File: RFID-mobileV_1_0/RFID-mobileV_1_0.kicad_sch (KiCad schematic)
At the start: 54 parts, among them J1 USB_C_Receptacle_USB2.0, J2 Conn_01x05_Male, J4 Conn_01x05_Male, Q1 MMBT3904, SW1 SW_Push, U1 XC6206P332MR, U2 E22-400T22S, U3 STM32G030FxP, U4 LM321, U5 DW02, U6 TP4054

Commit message: update
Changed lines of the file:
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@@
+    (stroke (width 0) (type default) (color 0 0 0 0))
+  )
+  (wire (pts (xy 85.09 53.975) (xy 85.09 52.07))
     (stroke (width 0) (type default) (color 0 0 0 0))
   )
@@
     (stroke (width 0) (type default) (color 0 0 0 0))
   )
+  (wire (pts (xy 80.645 52.07) (xy 80.645 53.975))
+    (stroke (width 0) (type default) (color 0 0 0 0))
+  )
   (wire (pts (xy 30.48 64.77) (xy 52.07 64.77))
     (stroke (width 0) (type solid) (color 0 0 0 0))
@@
     (stroke (width 0) (type default) (color 0 0 0 0))
   )
-  (wire (pts (xy 88.265 53.975) (xy 80.645 53.975))
-    (stroke (width 0) (type default) (color 0 0 0 0))
-  )
   (wire (pts (xy 80.645 153.67) (xy 80.645 156.21))
     (stroke (width 0) (type default) (color 0 0 0 0))
@@
     (stroke (width 0) (type default) (color 0 0 0 0))
   )
+  (wire (pts (xy 88.265 53.975) (xy 85.09 53.975))
+    (stroke (width 0) (type default) (color 0 0 0 0))
+  )
   (wire (pts (xy 49.53 93.345) (xy 49.53 95.885))
     (stroke (width 0) (type default) (color 0 0 0 0))
@@
     (stroke (width 0) (type solid) (color 0 0 0 0))
   )
-  (wire (pts (xy 80.645 51.435) (xy 80.645 53.975))
+  (wire (pts (xy 78.74 51.435) (xy 78.74 53.975))
     (stroke (width 0) (type default) (color 0 0 0 0))
   )
@@
   )
   (wire (pts (xy 86.995 87.63) (xy 86.995 90.17))
+    (stroke (width 0) (type default) (color 0 0 0 0))
+  )
+  (wire (pts (xy 78.74 53.975) (xy 80.645 53.975))
     (stroke (width 0) (type default) (color 0 0 0 0))
   )
@@
     (pin "4")
     (pin "5")
+  )
+  (symbol (lib_id "power:VCC") (at 80.645 52.07 0) (unit 1)
+    (in_bom yes) (on_board yes) (fields_autoplaced)
+    (property "Reference" "#PWR0102" (id 0) (at 80.645 55.88 0)
+      (effects (font (size 1.27 1.27)) hide)
+    )
+    (property "Value" "VCC" (id 1) (at 80.645 46.99 0))
+    (property "Footprint" "" (id 2) (at 80.645 52.07 0)
+      (effects (font (size 1.27 1.27)) hide)
+    )
+    (property "Datasheet" "" (id 3) (at 80.645 52.07 0)
+      (effects (font (size 1.27 1.27)) hide)
+    )
+    (pin "1")
   )
   (symbol (lib_id "Device:R") (at 130.175 92.075 0) (unit 1)
@@
     (pin "1")
     (pin "2")
+  )
+  (symbol (lib_id "power:VCC") (at 85.09 52.07 0) (unit 1)
+    (in_bom yes) (on_board yes) (fields_autoplaced)
+    (property "Reference" "#PWR0101" (id 0) (at 85.09 55.88 0)
+      (effects (font (size 1.27 1.27)) hide)
+    )
+    (property "Value" "" (id 1) (at 85.09 46.99 0))
+    (property "Footprint" "" (id 2) (at 85.09 52.07 0)
+      (effects (font (size 1.27 1.27)) hide)
+    )
+    (property "Datasheet" "" (id 3) (at 85.09 52.07 0)
+      (effects (font (size 1.27 1.27)) hide)
+    )
+    (pin "1")
   )
   (symbol (lib_id "Connector:TestPoint") (at 255.905 52.07 90) (unit 1)
@@
     (pin "2")
   )
-  (symbol (lib_id "power:+3V3") (at 80.645 51.435 0) (unit 1)
-    (in_bom yes) (on_board yes) (fields_autoplaced)
-    (property "Reference" "#PWR013" (id 0) (at 80.645 55.245 0)
-      (effects (font (size 1.27 1.27)) hide)
-    )
-    (property "Value" "+3V3" (id 1) (at 80.645 45.72 0))
-    (property "Footprint" "" (id 2) (at 80.645 51.435 0)
-      (effects (font (size 1.27 1.27)) hide)
-    )
-    (property "Datasheet" "" (id 3) (at 80.645 51.435 0)
+  (symbol (lib_id "power:+3V3") (at 78.74 51.435 0) (unit 1)
+    (in_bom yes) (on_board yes) (fields_autoplaced)
+    (property "Reference" "#PWR013" (id 0) (at 78.74 55.245 0)
+      (effects (font (size 1.27 1.27)) hide)
+    )
+    (property "Value" "+3V3" (id 1) (at 78.74 45.72 0))
+    (property "Footprint" "" (id 2) (at 78.74 51.435 0)
+      (effects (font (size 1.27 1.27)) hide)
+    )
+    (property "Datasheet" "" (id 3) (at 78.74 51.435 0)
       (effects (font (size 1.27 1.27)) hide)
     )
@@
       (reference "#PWR051") (unit 1) (value "GND") (footprint "")
     )
+    (path "/9f4d0c66-c958-4f69-b6e2-4c720641bae6"
+      (reference "#PWR0101") (unit 1) (value "VCC") (footprint "")
+    )
+    (path "/07dea2b7-24c3-46d3-9aab-8489613fedcc"
+      (reference "#PWR0102") (unit 1) (value "VCC") (footprint "")
+    )
     (path "/ac27cb01-7e08-4126-9053-c19587e4f0b6"

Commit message: update
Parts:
- AE1: value Antenna -> (none); footprint RF_Antenna:433MHz -> (none)
- J3: value (none) -> Conn_01x05_Female; footprint (none) -> Connector_PinHeader_2.54mm:PinHeader_1x05_P2.54mm_Vertical
- JP1, JP2, JP3, JP4: value (none) -> SolderJumper_2_Open; footprint (none) -> Jumper:SolderJumper-2_P1.3mm_Open_RoundedPad1.0x1.5mm
- TP1: value (none) -> RFID_TX; footprint (none) -> TestPoint:TestPoint_Pad_1.5x1.5mm
- TP2: value (none) -> 3.3V
- TP3: value (none) -> GND
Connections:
- net PA7: no longer D3.1 (K)
- net PA8: now also D2.1 (K); no longer D4.1 (K)
- net VBUS_sing: now also U3.13 (PA6); no longer U3.12 (PA5)
- net buz: now also U3.12 (PA5)
- net PA9: now reaches U3.16 (PA11[PA9])
- net PA9: now also D3.1 (K)
- net PA10: now reaches U3.17 (PA12[PA10])
- net PA10: now also D4.1 (K)
- removed net PA6: D2.1 (K), U3.13 (PA6)
- no-connect marks 12 -> 10
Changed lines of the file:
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@@
   (no_connect (at 88.265 45.085))
   (no_connect (at 88.265 47.625))
-  (no_connect (at 137.795 47.625))
-  (no_connect (at 137.795 50.165))
   (no_connect (at 255.905 31.75))
   (no_connect (at 39.37 50.8))
@@
     (stroke (width 0) (type solid) (color 0 0 0 0))
   )
+  (wire (pts (xy 137.795 50.165) (xy 150.495 50.165))
+    (stroke (width 0) (type default) (color 0 0 0 0))
+  )
   (polyline (pts (xy 60.325 124.46) (xy 108.585 124.46))
     (stroke (width 0) (type default) (color 0 0 0 0))
@@
     (stroke (width 0) (type default) (color 0 0 0 0))
   )
+  (wire (pts (xy 137.795 47.625) (xy 150.495 47.625))
+    (stroke (width 0) (type default) (color 0 0 0 0))
+  )
   (wire (pts (xy 198.755 33.02) (xy 198.755 29.845))
     (stroke (width 0) (type default) (color 0 0 0 0))
@@
     (stroke (width 0) (type default) (color 0 0 0 0))
   )
+  (wire (pts (xy 137.795 42.545) (xy 150.495 42.545))
+    (stroke (width 0) (type default) (color 0 0 0 0))
+  )
   (wire (pts (xy 222.885 134.62) (xy 222.885 135.255))
     (stroke (width 0) (type solid) (color 0 0 0 0))
@@
     (stroke (width 0) (type default) (color 0 0 0 0))
   )
-  (wire (pts (xy 137.795 42.545) (xy 150.495 42.545))
-    (stroke (width 0) (type default) (color 0 0 0 0))
-  )
   (polyline (pts (xy 187.96 77.47) (xy 238.125 77.47))
     (stroke (width 0) (type default) (color 0 0 0 0))
@@
     (effects (font (size 1.27 1.27)) (justify left bottom))
   )
-  (label "PA7" (at 222.885 158.115 0)
+  (label "PA9" (at 222.885 158.115 0)
     (effects (font (size 1.27 1.27)) (justify left bottom))
   )
@@
     (effects (font (size 1.27 1.27)) (justify right bottom))
   )
-  (label "PA6" (at 150.495 40.005 180)
+  (label "VBUS_sing" (at 150.495 40.005 180)
     (effects (font (size 1.27 1.27)) (justify right bottom))
   )
@@
   )
   (label "LoRa_RXD" (at 129.54 163.83 180)
+    (effects (font (size 1.27 1.27)) (justify right bottom))
+  )
+  (label "PA9" (at 150.495 47.625 180)
     (effects (font (size 1.27 1.27)) (justify right bottom))
   )
@@
     (effects (font (size 1.27 1.27)) (justify right bottom))
   )
-  (label "VBUS_sing" (at 150.495 37.465 180)
+  (label "buz" (at 150.495 37.465 180)
     (effects (font (size 1.27 1.27)) (justify right bottom))
   )
@@
     (effects (font (size 1.27 1.27)) (justify right bottom))
   )
-  (label "PA6" (at 212.725 158.115 0)
+  (label "PA8" (at 212.725 158.115 0)
     (effects (font (size 1.27 1.27)) (justify left bottom))
   )
@@
     (effects (font (size 1.27 1.27)) (justify right bottom))
   )
+  (label "PA10" (at 150.495 50.165 180)
+    (effects (font (size 1.27 1.27)) (justify right bottom))
+  )
   (label "NRST" (at 180.975 36.195 180)
     (effects (font (size 1.27 1.27)) (justify right bottom))
@@
     (effects (font (size 1.27 1.27)) (justify left bottom))
   )
+  (label "BATT_moint" (at 150.495 24.765 180)
+    (effects (font (size 1.27 1.27)) (justify right bottom))
+  )
   (label "PA7" (at 150.495 42.545 180)
-    (effects (font (size 1.27 1.27)) (justify right bottom))
-  )
-  (label "BATT_moint" (at 150.495 24.765 180)
     (effects (font (size 1.27 1.27)) (justify right bottom))
   )
@@
     (effects (font (size 1.27 1.27)) (justify right bottom))
   )
-  (label "PA8" (at 231.775 158.75 0)
+  (label "PA10" (at 231.775 158.75 0)
     (effects (font (size 1.27 1.27)) (justify left bottom))
   )
@@
     (in_bom no) (on_board yes)
     (property "Reference" "TP3" (id 0) (at 250.825 53.34 90))
-    (property "Value" "" (id 1) (at 246.38 55.245 90))
+    (property "Value" "GND" (id 1) (at 246.38 55.245 90))
     (property "Footprint" "TestPoint:TestPoint_Pad_1.5x1.5mm" (id 2) (at 255.905 50.165 0)
       (effects (font (size 1.27 1.27)) hide)
@@
     (in_bom no) (on_board yes)
     (property "Reference" "TP1" (id 0) (at 250.825 46.355 90))
-    (property "Value" "" (id 1) (at 246.38 48.26 90))
-    (property "Footprint" "" (id 2) (at 255.905 43.18 0)
+    (property "Value" "RFID_TX" (id 1) (at 246.38 48.26 90))
+    (property "Footprint" "TestPoint:TestPoint_Pad_1.5x1.5mm" (id 2) (at 255.905 43.18 0)
       (effects (font (size 1.27 1.27)) hide)
     )
@@
     (in_bom no) (on_board yes)
     (property "Reference" "JP4" (id 0) (at 116.84 165.1 0))
-    (property "Value" "" (id 1) (at 125.095 168.275 0)
-      (effects (font (size 1.27 1.27)) hide)
-    )
-    (property "Footprint" "" (id 2) (at 114.935 166.37 0)
+    (property "Value" "SolderJumper_2_Open" (id 1) (at 125.095 168.275 0)
+      (effects (font (size 1.27 1.27)) hide)
+    )
+    (property "Footprint" "Jumper:SolderJumper-2_P1.3mm_Open_RoundedPad1.0x1.5mm" (id 2) (at 114.935 166.37 0)
       (effects (font (size 1.27 1.27)) hide)
     )
@@
       (effects (font (size 1.27 1.27)) hide)
     )
-    (property "Value" "" (id 1) (at 85.09 46.99 0))
+    (property "Value" "VCC" (id 1) (at 85.09 46.99 0))
     (property "Footprint" "" (id 2) (at 85.09 52.07 0)
       (effects (font (size 1.27 1.27)) hide)
@@
     (in_bom no) (on_board yes)
     (property "Reference" "TP2" (id 0) (at 250.825 50.165 90))
-    (property "Value" "" (id 1) (at 246.38 52.07 90))
+    (property "Value" "3.3V" (id 1) (at 246.38 52.07 90))
     (property "Footprint" "TestPoint:TestPoint_Pad_1.5x1.5mm" (id 2) (at 255.905 46.99 0)
       (effects (font (size 1.27 1.27)) hide)
@@
     (in_bom no) (on_board yes)
     (property "Reference" "JP2" (id 0) (at 116.84 160.02 0))
-    (property "Value" "" (id 1) (at 125.095 163.195 0)
-      (effects (font (size 1.27 1.27)) hide)
-    )
-    (property "Footprint" "" (id 2) (at 114.935 161.29 0)
+    (property "Value" "SolderJumper_2_Open" (id 1) (at 125.095 163.195 0)
+      (effects (font (size 1.27 1.27)) hide)
+    )
+    (property "Footprint" "Jumper:SolderJumper-2_P1.3mm_Open_RoundedPad1.0x1.5mm" (id 2) (at 114.935 161.29 0)
       (effects (font (size 1.27 1.27)) hide)
     )
@@
       (effects (font (size 1.27 1.27)) (justify left))
     )
-    (property "Value" "Antenna" (id 1) (at 123.19 144.1449 0)
-      (effects (font (size 1.27 1.27)) (justify left))
-    )
-    (property "Footprint" "RF_Antenna:433MHz" (id 2) (at 120.65 142.24 0)
+    (property "Value" "" (id 1) (at 123.19 144.1449 0)
+      (effects (font (size 1.27 1.27)) (justify left))
+    )
+    (property "Footprint" "" (id 2) (at 120.65 142.24 0)
       (effects (font (size 1.27 1.27)) hide)
     )
@@
       (effects (font (size 1.27 1.27)) (justify left))
     )
-    (property "Value" "" (id 1) (at 203.835 45.085 0)
-      (effects (font (size 1.27 1.27)) (justify left))
-    )
-    (property "Footprint" "" (id 2) (at 217.805 38.1 0)
+    (property "Value" "Conn_01x05_Female" (id 1) (at 203.835 45.085 0)
+      (effects (font (size 1.27 1.27)) (justify left))
+    )
+    (property "Footprint" "Connector_PinHeader_2.54mm:PinHeader_1x05_P2.54mm_Vertical" (id 2) (at 217.805 38.1 0)
       (effects (font (size 1.27 1.27)) hide)
     )
@@
     (in_bom no) (on_board yes)
     (property "Reference" "JP1" (id 0) (at 116.84 157.48 0))
-    (property "Value" "" (id 1) (at 125.095 160.655 0)
-      (effects (font (size 1.27 1.27)) hide)
-    )
-    (property "Footprint" "" (id 2) (at 114.935 158.75 0)
+    (property "Value" "SolderJumper_2_Open" (id 1) (at 125.095 160.655 0)
+      (effects (font (size 1.27 1.27)) hide)
+    )
+    (property "Footprint" "Jumper:SolderJumper-2_P1.3mm_Open_RoundedPad1.0x1.5mm" (id 2) (at 114.935 158.75 0)
       (effects (font (size 1.27 1.27)) hide)
     )
@@
     (in_bom no) (on_board yes)
     (property "Reference" "JP3" (id 0) (at 116.84 162.56 0))
-    (property "Value" "" (id 1) (at 125.73 161.925 0)
-      (effects (font (size 1.27 1.27)) hide)
-    )
-    (property "Footprint" "" (id 2) (at 114.935 163.83 0)
+    (property "Value" "SolderJumper_2_Open" (id 1) (at 125.73 161.925 0)
+      (effects (font (size 1.27 1.27)) hide)
+    )
+    (property "Footprint" "Jumper:SolderJumper-2_P1.3mm_Open_RoundedPad1.0x1.5mm" (id 2) (at 114.935 163.83 0)
       (effects (font (size 1.27 1.27)) hide)
     )
@@
     )
     (path "/ac27cb01-7e08-4126-9053-c19587e4f0b6"
-      (reference "AE1") (unit 1) (value "Antenna") (footprint "RF_Antenna:433MHz")
+      (reference "AE1") (unit 1) (value "Antenna") (footprint "RF_Antenna:433MHz_V")
     )
     (path "/2984ca69-dc32-4c20-a11b-903dd74ada01"

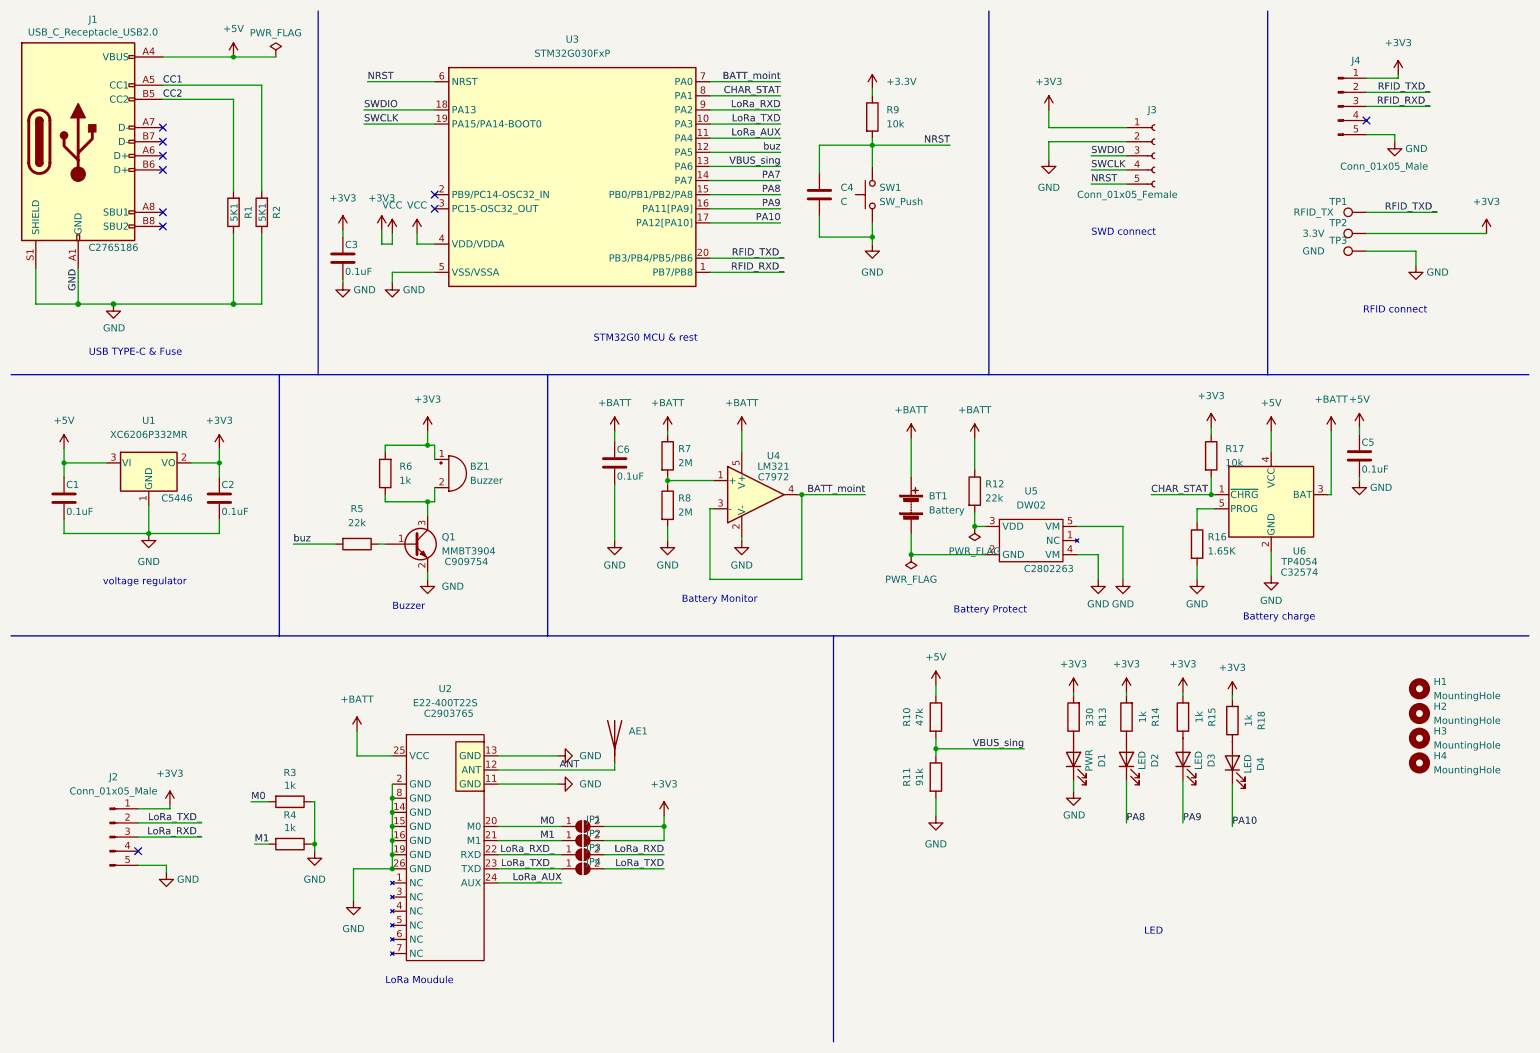
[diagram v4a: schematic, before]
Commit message: update
remote DW02
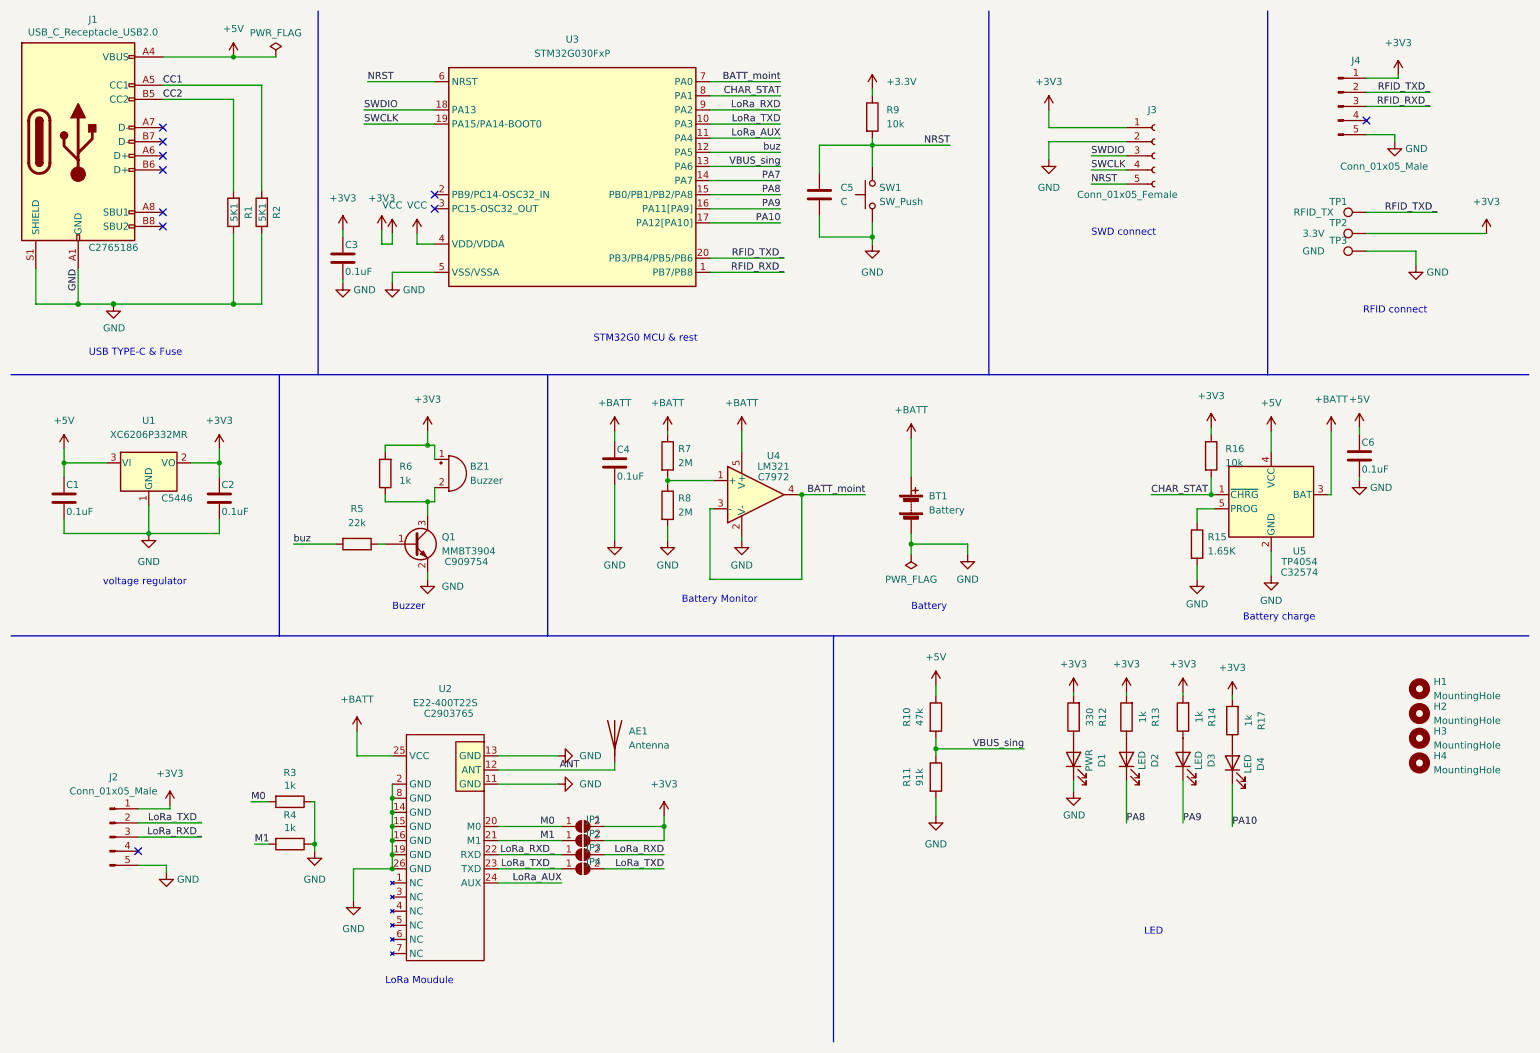
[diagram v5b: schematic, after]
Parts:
- removed R12: 22k, Resistor_SMD:R_0805_2012Metric, symbol Device:R
- removed U5: DW02, Package_TO_SOT_SMD:SOT-23-5, symbol Battery_Management:DW02
- AE1: value (none) -> Antenna; footprint (none) -> RF_Antenna:433MHz_V
- renumbered C6 to C4, C4 to C5, C5 to C6, R13 to R12, R14 to R13, R15 to R14, R16 to R15, R17 to R16, R18 to R17, U6 to U5
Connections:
- net GND: now also BT1.2 (-)
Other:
- note added: "Battery"
- note removed: "Battery Protect"
